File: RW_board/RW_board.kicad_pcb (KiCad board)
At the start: 4 copper layers, 45.6 x 45.6 mm, 116 parts, among them IC201 MAX44284WAUT+T, IC301 MCT8316Z0RQRGFRQ1, J1 Conn_01x08_Pin, J2 1-84953-1, J401 USB4105-GF-A, J402 20021521-00010T4LF, Q201 BSZ300N15NS5ATMA1, SW401 SW_Push, U201 LM5022MM, U401 ATSAMD21G18A-M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

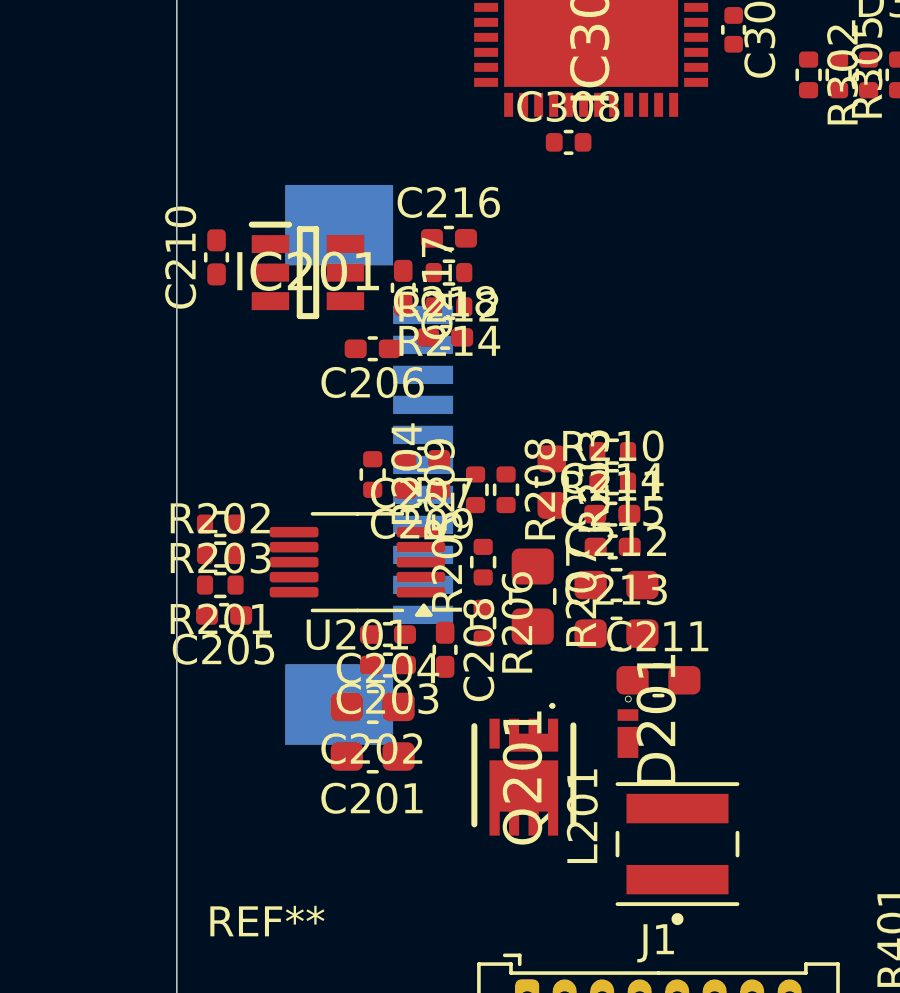
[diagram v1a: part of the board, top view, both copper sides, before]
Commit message: Some more boost changes
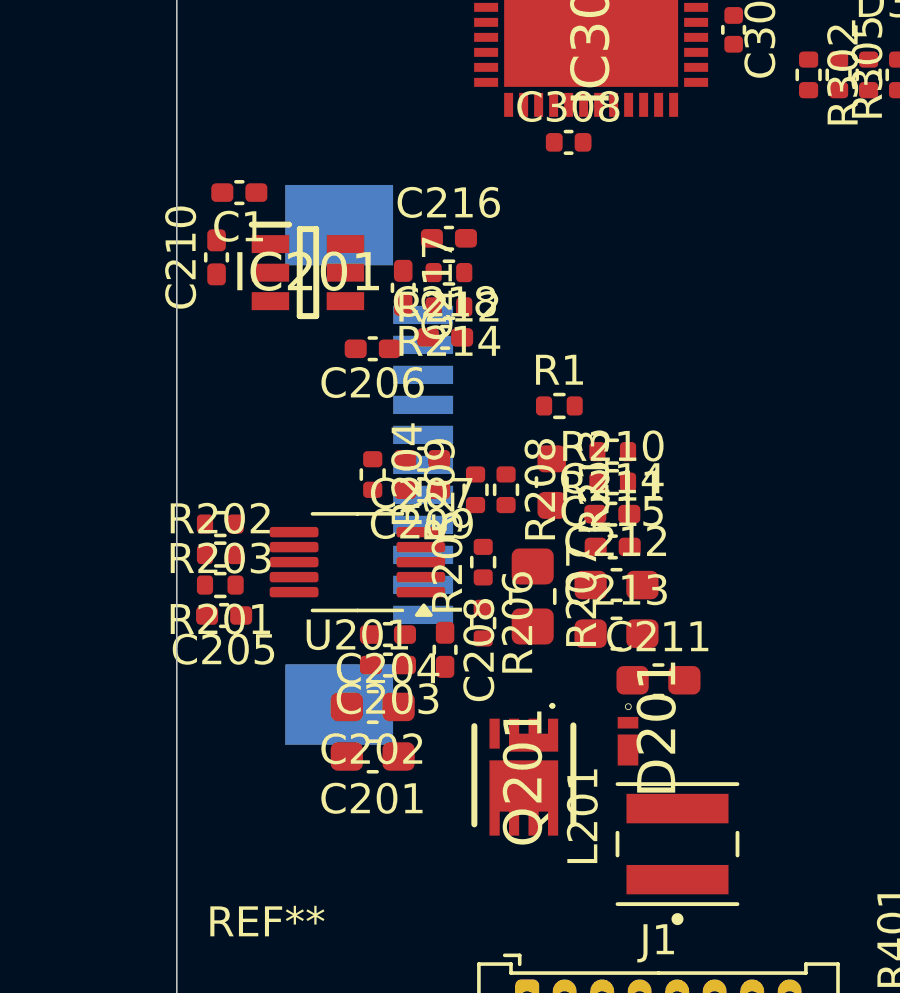
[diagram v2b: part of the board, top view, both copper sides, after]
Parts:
- added C1: 4.7u, Capacitor_SMD:C_0402_1005Metric_Pad0.74x0.62mm_HandSolder, F.Cu at (128.5, 90.4)
- added R1: 20, Resistor_SMD:R_0402_1005Metric, F.Cu at (139.2, 97.5)
- D201: footprint RW_Imports:X3-WLB1608-2 -> Senior Design:X3-WLB1608-2
- D401: footprint RW_Imports:PRTR5V0U2X -> Senior Design:PRTR5V0U2X
- IC201: footprint RW_Imports:SOT95P280X145-6N -> Senior Design:SOT95P280X145-6N
- IC301: footprint RW_Imports:QFN50P500X700X100-41N-D -> Senior Design:QFN50P500X700X100-41N-D
- J2: footprint RW_Imports:1849531 -> Senior Design:1849531
- J402: footprint RW_Imports:2002152100010T4LF -> Senior Design:2002152100010T4LF
- Q201: footprint RW_Imports:BSZ300N15NS5ATMA1 -> Senior Design:BSZ300N15NS5ATMA1
- Y401: footprint RW_Imports:830105946101 -> Senior Design:830105946101
- moved D201 0.25 mm to (141.5, 108.7)
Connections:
- L201 pad 2: Net-(Q201-GATE) -> /Buck-Boost/Drain
- R208 pad 2: Net-(D201-K) -> Net-(R1-Pad1)

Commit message: Initial routing complete
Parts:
- removed R301: 0R, Capacitor_SMD:C_0201_0603Metric
- removed TP1, TP10, TP11, TP12, TP13, TP14, TP15, TP16, TP17, TP18, TP19, TP2, TP20, TP21, TP22, TP3, TP4, TP5, TP6, TP7, TP8, TP9: TestPoint, TestPoint:TestPoint_Pad_1.0x1.0mm
- added REF**: MountingHole_6.4mm_M6, MountingHole:MountingHole_6.4mm_M6, F.Cu at (149.2, 99.6)
- D201: footprint Senior Design:X3-WLB1608-2 -> RW_Imports:X3-WLB1608-2
- D401: footprint Senior Design:PRTR5V0U2X -> RW_Imports:PRTR5V0U2X
- IC201: footprint Senior Design:SOT95P280X145-6N -> RW_Imports:SOT95P280X145-6N
- IC301: footprint Senior Design:QFN50P500X700X100-41N-D -> RW_Imports:QFN50P500X700X100-41N-D
- J2: footprint Senior Design:1849531 -> RW_Imports:1849531
- J402: footprint Senior Design:2002152100010T4LF -> RW_Imports:2002152100010T4LF
- Q201: footprint Senior Design:BSZ300N15NS5ATMA1 -> RW_Imports:BSZ300N15NS5ATMA1
- Y401: footprint Senior Design:830105946101 -> RW_Imports:830105946101
- moved J402 15.1 mm to (167.6, 105.7)
- moved SW401 10.4 mm to (169.8, 90.3)
- moved R403 10.4 mm to (169.7, 96.9)
- moved C206 9.37 mm to (129.7, 104.4), turned to -90 degrees
- moved C211 8.51 mm to (139.1, 98.9)
- moved R208 7.85 mm to (131.5, 95.1), turned to 0 degrees
- moved R304 7.24 mm to (143.8, 89.2), turned to 90 degrees
- moved R1 6.43 mm to (133.0, 95.7), turned to -90 degrees
- moved R209 6.41 mm to (131.5, 96.2), turned to 180 degrees
- moved L201 6.00 mm to (137.2, 111.5)
- moved C215 5.12 mm to (139.1, 97.5)
- moved R211 5.12 mm to (139.1, 94.3)
- moved C214 5.12 mm to (139.1, 96.4)
- moved R210 5.12 mm to (139.1, 95.3)
- moved R402 4.83 mm to (166.1, 95.9), turned to 90 degrees
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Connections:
- net Net-(IC201-RS+) renamed /Buck-Boost/Sense+
- net Net-(IC201-RS-) renamed /Buck-Boost/Sense-
- net Net-(U201-FB) renamed /Buck-Boost/Feedback
- net Net-(U201-UVLO) renamed /Buck-Boost/UVLO
- C301 pad 2: GNDPWR -> GND
- C302 pad 2: GNDPWR -> GND
- C304 pad 2: GNDPWR -> GND
- C305 pad 2: GNDPWR -> GND
- D303 pad 1: GNDPWR -> GND
- IC301 pad 12: GNDPWR -> GND
- IC301 pad 15: GNDPWR -> GND
- IC301 pad 18: GNDPWR -> GND
- J1 pad 6: /RX -> /TX
- U401 pad 37: /RX -> /TX
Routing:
- net GND: track 0.00 -> 107.6 mm, vias 0 -> 42
- net VDC: track 0.00 -> 54.9 mm, vias 0 -> 2
- net /RX: track 0.00 -> 54.7 mm, vias 0 -> 1
- net /TX: track 0.00 -> 51.8 mm, vias 0 -> 1
- net /MCU/Motor_nFAULT: track 0.00 -> 44.2 mm, vias 0 -> 2
- net /MCU/D_P: track 0.00 -> 39.0 mm
- net /MCU/SWCLK: track 0.00 -> 37.9 mm, vias 0 -> 1
- net /MCU/D_N: track 0.00 -> 37.3 mm
- net /Buck-Boost/CURRENTSENSE: track 0.00 -> 36.7 mm, vias 0 -> 2
- net /MCU/SWDIO: track 0.00 -> 33.7 mm, vias 0 -> 1
- net +3.3V: track 0.00 -> 33.6 mm, vias 0 -> 9
- net /Buck-Boost/VSENSE: track 0.00 -> 31.9 mm, vias 0 -> 2
- net /MCU/MISO: track 0.00 -> 28.4 mm, vias 0 -> 2
- net /MCU/MOTOR_DRVOFF: track 0.00 -> 28.0 mm, vias 0 -> 2
- net /MCU/MOTOR_SPEED: track 0.00 -> 27.5 mm, vias 0 -> 2
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- added copper zone on In2.Cu, net +3.3V
- added copper zone on F.Cu, net /Buck-Boost/24V_OUT
- added copper zone on In2.Cu, net /Buck-Boost/24V_OUT
- added copper zone on F.Cu, net /Buck-Boost/Drain
- added copper zone on F.Cu, net /Buck-Boost/Source
- added copper zone on In2.Cu, net /Motor Driver/FB_BK
- added copper zone on B.Cu, net /Motor Driver/OUTA
- added copper zone on F.Cu, net /Motor Driver/OUTA
- added copper zone on B.Cu, net /Motor Driver/OUTB
- added copper zone on F.Cu, net /Motor Driver/OUTB
- added copper zone on B.Cu, net /Motor Driver/OUTC
- added copper zone on F.Cu, net /Motor Driver/OUTC
- added copper zone on F.Cu, net GND
- added copper zone on In1.Cu, net GND
- added copper zone on F.Cu, net Net-(D201-K)
- added copper zone on F.Cu, net VDC
- removed copper zone on In1.Cu, net GNDPWR

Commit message: Board complete
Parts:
- removed the REF** at (129.4, 79.6)
- removed the REF** at (169.0, 79.6)
- removed the REF** at (169.0, 119.3)
- removed the REF** at (129.4, 119.3)
- added H101: MountingHole_Pad, RW_Imports:MountingHole_3.4mm_Pad, F.Cu at (129.4, 79.6)
- added H102: MountingHole_Pad, RW_Imports:MountingHole_3.4mm_Pad, F.Cu at (169.0, 79.6)
- added H103: MountingHole_Pad, RW_Imports:MountingHole_3.4mm_Pad, F.Cu at (129.4, 119.3)
- added H104: MountingHole_Pad, RW_Imports:MountingHole_3.4mm_Pad, F.Cu at (169.0, 119.3)
- added R103: DNP, Resistor_SMD:R_0402_1005Metric, F.Cu at (129.2, 84.2)
- added R104: DNP, Resistor_SMD:R_0402_1005Metric, F.Cu at (164.5, 79.6)
- added R105: DNP, Resistor_SMD:R_0402_1005Metric, F.Cu at (134.0, 119.3)
- added R106: DNP, Resistor_SMD:R_0402_1005Metric, F.Cu at (169.0, 114.7)
- added TP1: TestPoint, TestPoint:TestPoint_Pad_1.0x1.0mm, B.Cu at (132.8, 88.0)
- added TP11: TestPoint, TestPoint:TestPoint_Pad_1.0x1.0mm, B.Cu at (154.8, 86.6)
- added TP12: TestPoint, TestPoint:TestPoint_Pad_1.0x1.0mm, B.Cu at (154.1, 92.2)
- added TP13: TestPoint, TestPoint:TestPoint_Pad_1.0x1.0mm, B.Cu at (154.4, 82.5)
- added TP14: TestPoint, TestPoint:TestPoint_Pad_1.0x1.0mm, B.Cu at (143.8, 92.6)
- added TP15: TestPoint, TestPoint:TestPoint_Pad_1.0x1.0mm, B.Cu at (152.9, 84.6)
- added TP16: TestPoint, TestPoint:TestPoint_Pad_1.0x1.0mm, B.Cu at (162.6, 93.0)
- added TP17: TestPoint, TestPoint:TestPoint_Pad_1.0x1.0mm, B.Cu at (147.7, 87.2)
- added TP18: TestPoint, TestPoint:TestPoint_Pad_1.0x1.0mm, B.Cu at (148.7, 91.3)
- added TP19: TestPoint, TestPoint:TestPoint_Pad_1.0x1.0mm, B.Cu at (151.9, 88.1)
- added TP2: TestPoint, TestPoint:TestPoint_Pad_1.0x1.0mm, B.Cu at (136.1, 88.0)
- added TP20: TestPoint, TestPoint:TestPoint_Pad_1.0x1.0mm, B.Cu at (168.5, 90.6)
- added TP21: TestPoint, TestPoint:TestPoint_Pad_1.0x1.0mm, B.Cu at (168.5, 92.6)
- added TP22: TestPoint, TestPoint:TestPoint_Pad_1.0x1.0mm, B.Cu at (147.7, 89.3)
- added TP23: TestPoint, TestPoint:TestPoint_Pad_1.0x1.0mm, F.Cu at (133.2, 106.6)
- added TP24: TestPoint, TestPoint:TestPoint_Pad_1.0x1.0mm, B.Cu at (142.7, 78.4)
- added TP25: TestPoint, TestPoint:TestPoint_Pad_1.0x1.0mm, F.Cu at (140.7, 107.7)
- added TP26: TestPoint, TestPoint:TestPoint_Pad_1.0x1.0mm, F.Cu at (127.9, 96.0)
- added TP3: TestPoint, TestPoint:TestPoint_Pad_1.0x1.0mm, B.Cu at (139.4, 88.0)
- added TP4: TestPoint, TestPoint:TestPoint_Pad_1.0x1.0mm, B.Cu at (141.0, 94.6)
- added TP5: TestPoint, TestPoint:TestPoint_Pad_1.0x1.0mm, B.Cu at (140.3, 90.9)
- added TP6: TestPoint, TestPoint:TestPoint_Pad_1.0x1.0mm, B.Cu at (142.7, 96.7)
- added TP7: TestPoint, TestPoint:TestPoint_Pad_1.0x1.0mm, B.Cu at (142.7, 80.4)
- added TP8: TestPoint, TestPoint:TestPoint_Pad_1.0x1.0mm, B.Cu at (161.2, 80.5)
- added TP9: TestPoint, TestPoint:TestPoint_Pad_1.0x1.0mm, B.Cu at (160.4, 87.0)
- moved C304 3.51 mm to (134.5, 83.4), turned to -90 degrees
- moved C305 2.19 mm to (133.0, 82.7), turned to -90 degrees
- moved R208 1.12 mm to (131.5, 96.3)
- moved R209 1.04 mm to (131.5, 95.1)
- moved C202 0.64 mm to (131.8, 112.6)
- moved C201 0.63 mm to (131.8, 114.3)
- moved C406 0.17 mm to (165.4, 84.2)
- moved C408 0.17 mm to (165.4, 85.2)
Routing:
- net Net-(H101-Pad1): track 0.00 -> 4.89 mm
- net Net-(H104-Pad1): track 0.00 -> 4.78 mm
- net Net-(H103-Pad1): track 0.00 -> 4.78 mm
- net Net-(H102-Pad1): track 0.00 -> 4.78 mm
- net /MCU/MOSI: track 23.6 -> 28.3 mm
- net /MCU/SCK: track 23.8 -> 27.8 mm
- net /Motor Driver/H_A: track 22.3 -> 26.1 mm, vias 1 -> 3
- net Net-(Q201-GATE): track 6.36 -> 9.90 mm
- net +3.3V: track 33.6 -> 36.9 mm
- net /MCU/MOTOR_nSLEEP: track 26.7 -> 29.0 mm
- net /MCU/SWCLK: track 37.9 -> 36.3 mm
- net /MCU/SWDIO: track 33.7 -> 32.4 mm
- net /Motor Driver/FB_BK: track 14.4 -> 15.6 mm
- net VDC: track 54.9 -> 55.9 mm
- net GND: track 107.6 -> 106.8 mm
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- added copper zone on B.Cu, net GND
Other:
- board text added: "+24V"
- board text added: "+3.3V"
- board text added: "+5V"
- board text added: "24V"
- board text added: "3.3V"
- board text added: "5V"
- board text added: "A"
- board text added: "B"
- board text added: "BRAKE"
- board text added: "C"
- board text added: "CS"
- board text added: "DRAIN"
- board text added: "DRVOFF"
- board text added: "FAULT"
- board text added: "GATE"
- board text added: "GND"
- board text added: "H_A"
- board text added: "H_B"
- board text added: "H_C"
- board text added: "ILIM"
- board text added: "ISENSE"
- board text added: "MISO"
- board text added: "MOSI"
- board text added: "NSLEEP"
- board text added: "PWM"
- board text added: "RX"
- board text added: "Reaction Wheel Board V1"
- board text added: "SCK"
- board text added: "SPEED"
- board text added: "TX"
- board text added: "VIN"
- board text added: "VSENSE"
- board text added: "nFAULT"

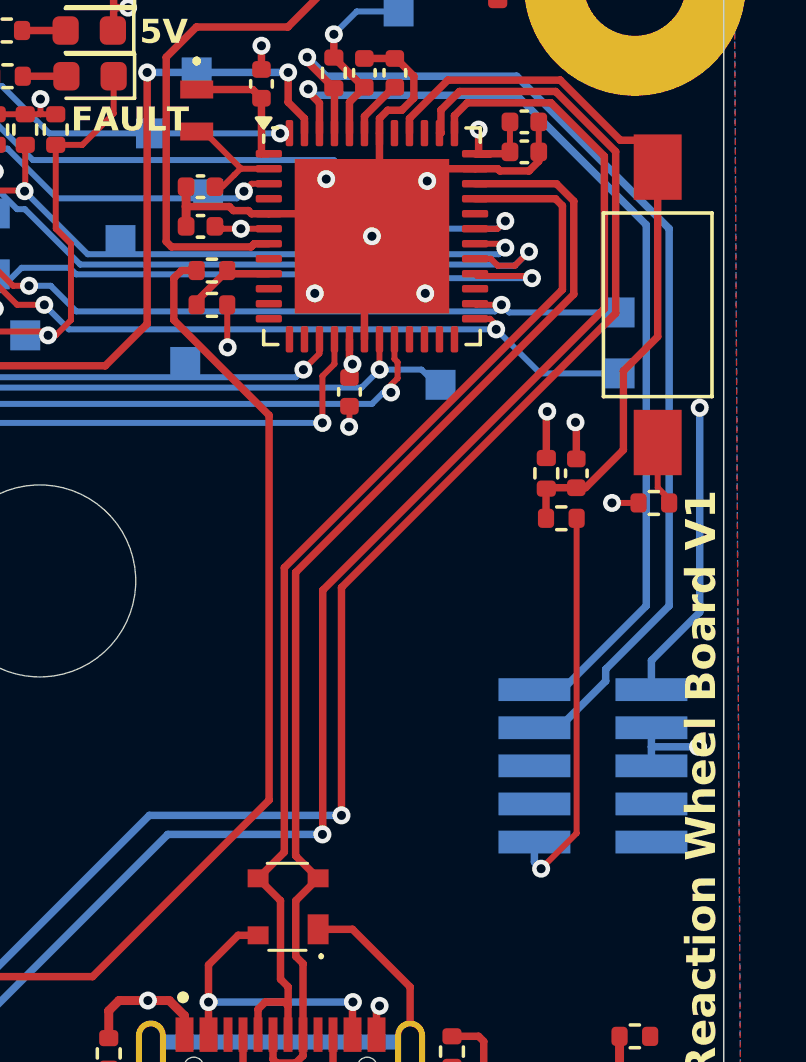
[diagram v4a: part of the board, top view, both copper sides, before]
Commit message: Added logo, TVS diode, made test production files
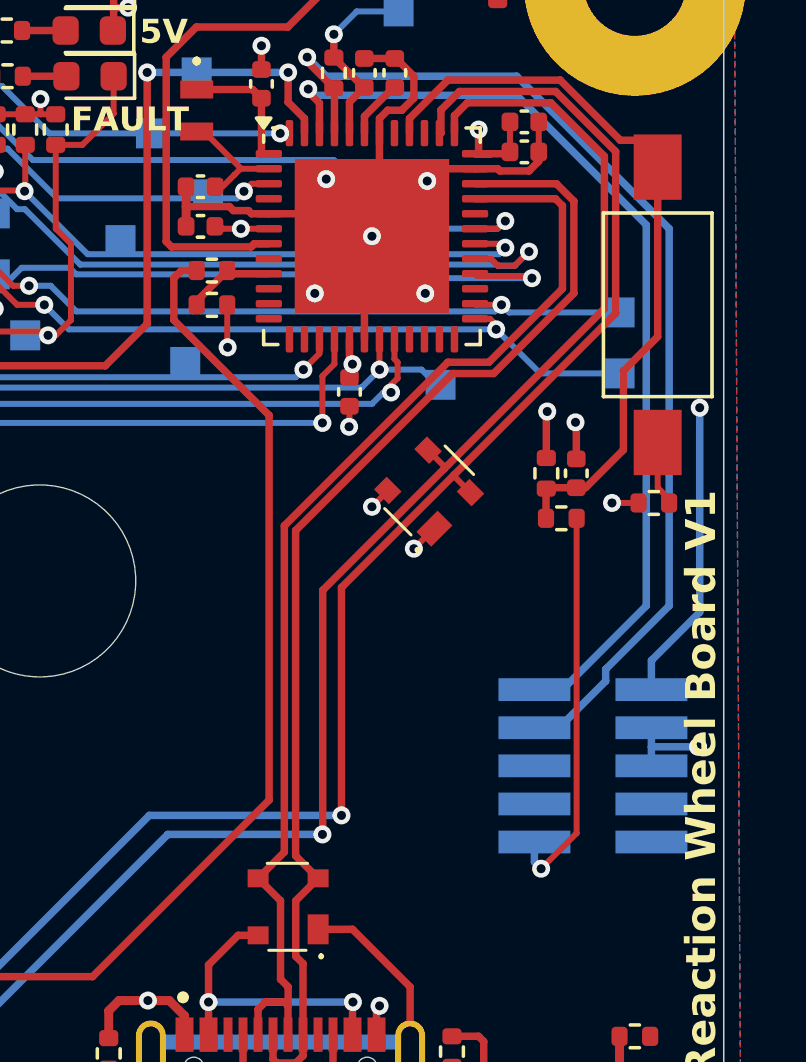
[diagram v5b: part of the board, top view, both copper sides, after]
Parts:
- added D403: PRTR5V0U2X,215, RW_Imports:PRTR5V0U2X, F.Cu at (162.2, 96.5)
- added G***: LOGO, RW_Imports:logo, B.Cu at (157.9, 104.2)
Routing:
- net GND: track 106.8 -> 107.8 mm, vias 42 -> 43
- net /TX: track 51.3 -> 52.1 mm
- net /RX: track 54.1 -> 54.9 mm
- net /MCU/D_P: track 38.6 -> 39.4 mm
- net /MCU/D_N: track 37.3 -> 38.1 mm
- net +3.3V: track 36.9 -> 37.7 mm, vias 9 -> 10

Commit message: via fix
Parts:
- moved TP11 0.25 mm to (155.1, 86.6)
- moved C305 0.13 mm to (133.0, 82.8)
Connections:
- D401 pad 1: /MCU/SHIELD -> GND
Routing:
- net /MCU/SHIELD: track 26.2 -> 20.2 mm
- net GND: track 107.8 -> 105.2 mm, vias 43 -> 50
- net VDC: track 55.9 -> 55.4 mm
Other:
- board text added: "nSLEEP"
- board text removed: "NSLEEP"

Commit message: Update mounting holes
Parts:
- H101, H102, H103, H104: footprint RW_Imports:MountingHole_3.4mm_Pad -> MountingHole:MountingHole_3.5mm_Pad_Via

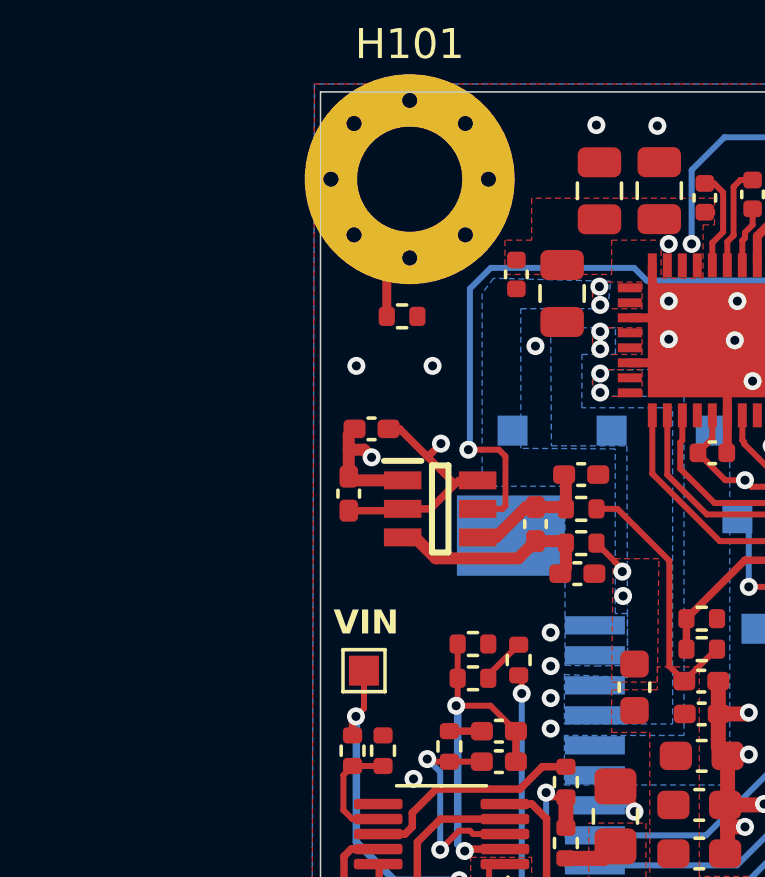
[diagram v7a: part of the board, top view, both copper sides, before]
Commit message: Boost Testpoint Update
2 Testpoints added to schematic and layout
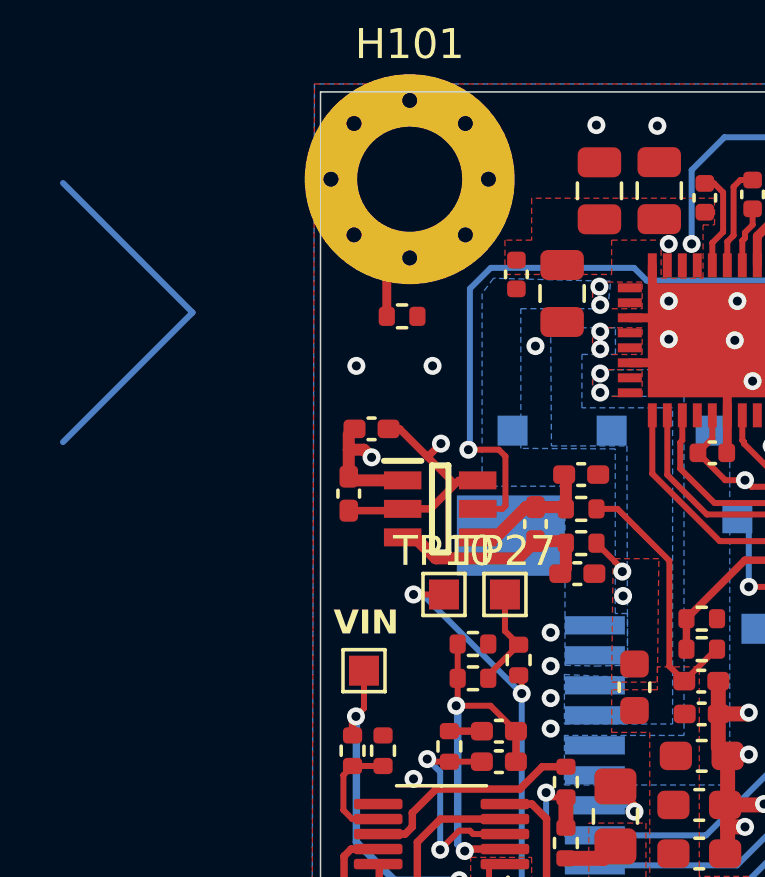
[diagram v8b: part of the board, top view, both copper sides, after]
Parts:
- added TP10: TestPoint, TestPoint:TestPoint_Pad_1.0x1.0mm, F.Cu at (130.6, 93.5)
- added TP27: TestPoint, TestPoint:TestPoint_Pad_1.0x1.0mm, F.Cu at (132.6, 93.5)
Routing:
- net Net-(D201-K): track 24.9 -> 43.1 mm, vias 2 -> 3
- net Net-(R1-Pad1): track 1.54 -> 3.40 mm
